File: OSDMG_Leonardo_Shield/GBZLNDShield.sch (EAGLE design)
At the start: 12 parts

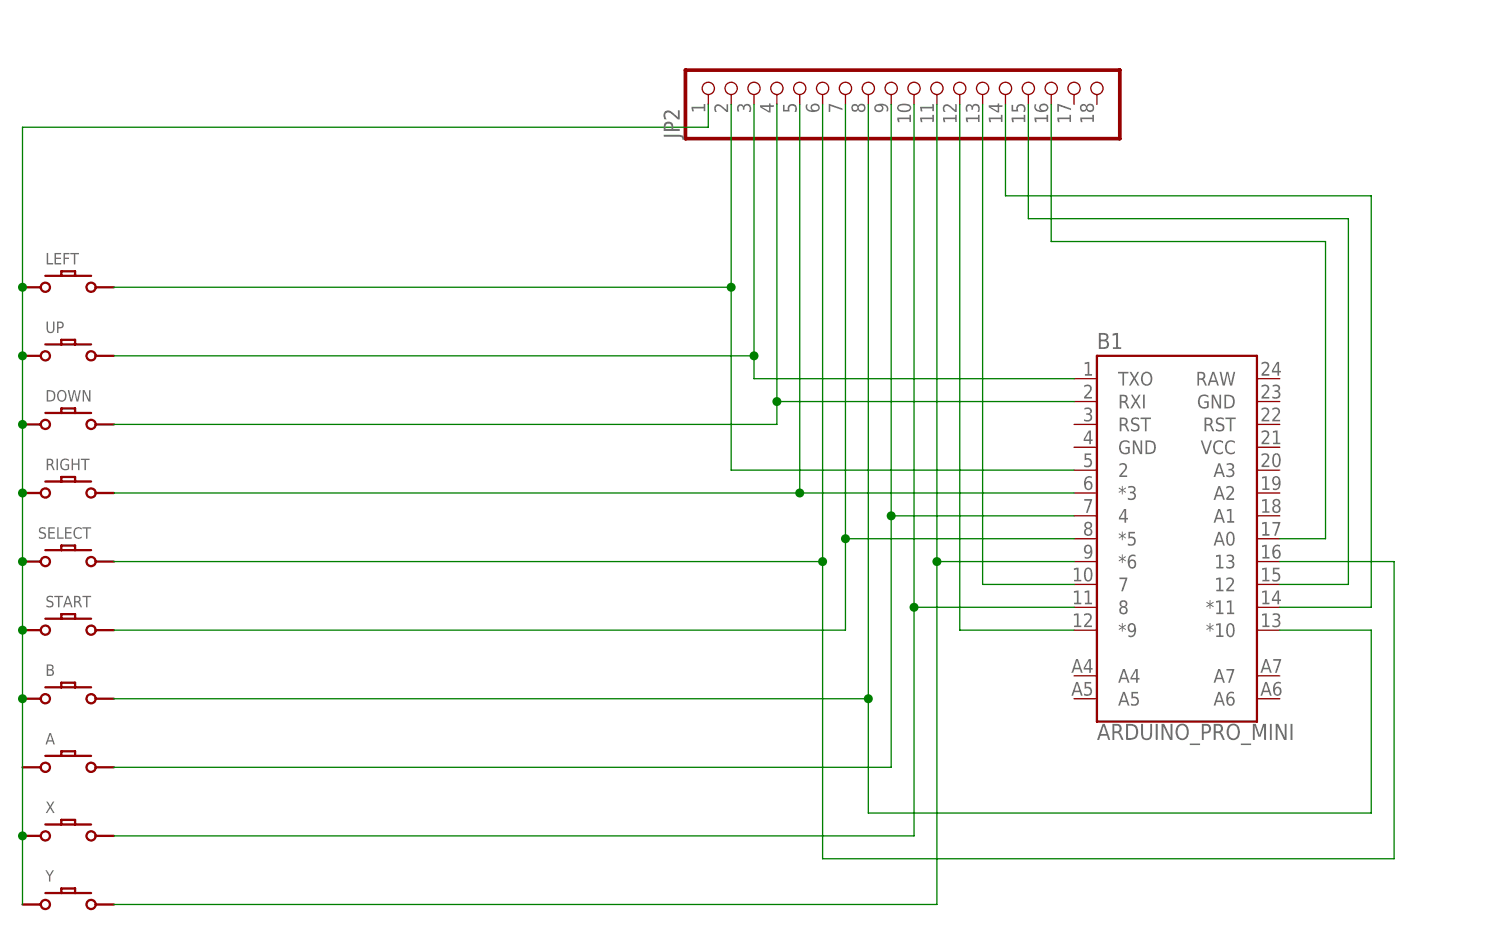
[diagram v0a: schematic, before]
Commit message: update board
5V and GND Pads and better placement of the leonardo
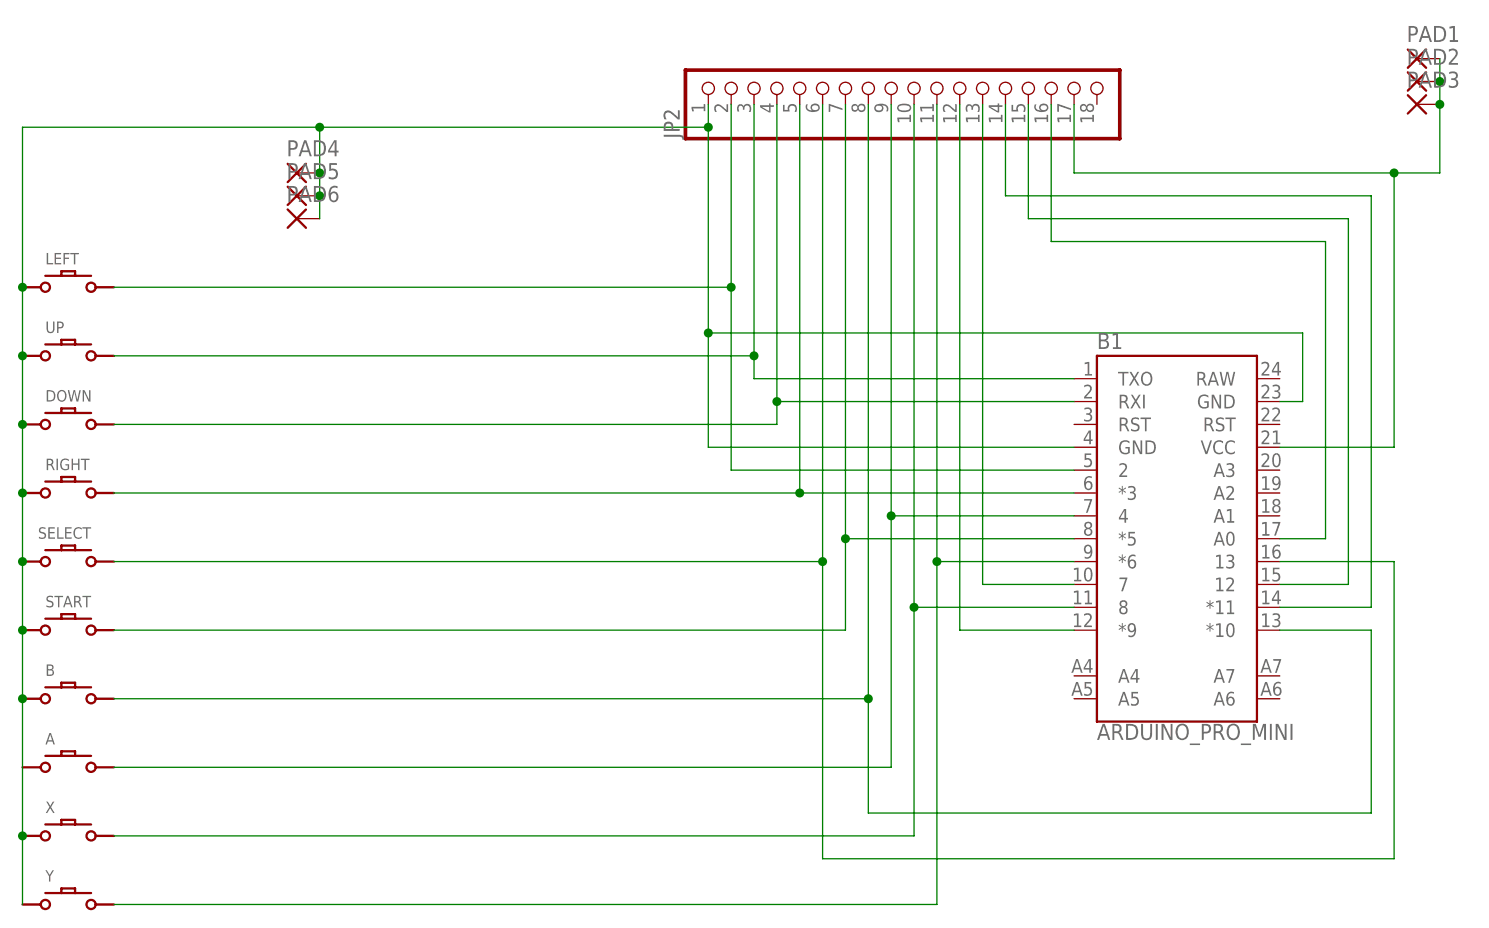
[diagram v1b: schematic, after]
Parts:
- added PAD1, PAD2, PAD3, PAD4, PAD5, PAD6: (no value), wirepad:SMD5
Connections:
- new net N$17: B1.VCC, JP2.17, PAD1.P, PAD2.P, PAD3.P
- net GND: now also B1.GND, B1.GND@2, PAD4.P, PAD5.P, PAD6.P
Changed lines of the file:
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@@
 <part name="JP2" library="adafruit" deviceset="PINHD-1X18" device="-BIG"/>
 <part name="B1" library="SparkFun-Boards" deviceset="ARDUINO_PRO_MINI" device=""/>
+<part name="PAD1" library="wirepad" library_urn="urn:adsk.eagle:library:412" deviceset="SMD5" device="" package3d_urn="urn:adsk.eagle:package:30841/1"/>
+<part name="PAD2" library="wirepad" library_urn="urn:adsk.eagle:library:412" deviceset="SMD5" device="" package3d_urn="urn:adsk.eagle:package:30841/1"/>
+<part name="PAD3" library="wirepad" library_urn="urn:adsk.eagle:library:412" deviceset="SMD5" device="" package3d_urn="urn:adsk.eagle:package:30841/1"/>
+<part name="PAD4" library="wirepad" library_urn="urn:adsk.eagle:library:412" deviceset="SMD5" device="" package3d_urn="urn:adsk.eagle:package:30841/1"/>
+<part name="PAD5" library="wirepad" library_urn="urn:adsk.eagle:library:412" deviceset="SMD5" device="" package3d_urn="urn:adsk.eagle:package:30841/1"/>
+<part name="PAD6" library="wirepad" library_urn="urn:adsk.eagle:library:412" deviceset="SMD5" device="" package3d_urn="urn:adsk.eagle:package:30841/1"/>
 </parts>
 <sheets>
@@
 <instance part="JP2" gate="A" x="109.22" y="91.44" rot="R90"/>
 <instance part="B1" gate="G$1" x="139.7" y="40.64"/>
+<instance part="PAD1" gate="1" x="167.64" y="93.98"/>
+<instance part="PAD2" gate="1" x="167.64" y="91.44"/>
+<instance part="PAD3" gate="1" x="167.64" y="88.9"/>
+<instance part="PAD4" gate="1" x="43.18" y="81.28"/>
+<instance part="PAD5" gate="1" x="43.18" y="78.74"/>
+<instance part="PAD6" gate="1" x="43.18" y="76.2"/>
 </instances>
 <busses>
@@
 <wire x1="12.7" y1="68.58" x2="12.7" y2="86.36" width="0.1524" layer="91"/>
 <pinref part="UP" gate="G$1" pin="P$1"/>
-<wire x1="12.7" y1="86.36" x2="88.9" y2="86.36" width="0.1524" layer="91"/>
+<wire x1="12.7" y1="86.36" x2="45.72" y2="86.36" width="0.1524" layer="91"/>
+<wire x1="45.72" y1="86.36" x2="88.9" y2="86.36" width="0.1524" layer="91"/>
 <wire x1="12.7" y1="60.96" x2="12.7" y2="68.58" width="0.1524" layer="91"/>
 <junction x="12.7" y="68.58"/>
@@
 <wire x1="88.9" y1="86.36" x2="88.9" y2="88.9" width="0.1524" layer="91"/>
 <pinref part="JP2" gate="A" pin="1"/>
+<pinref part="PAD6" gate="1" pin="P"/>
+<pinref part="PAD5" gate="1" pin="P"/>
+<wire x1="45.72" y1="76.2" x2="45.72" y2="78.74" width="0.1524" layer="91"/>
+<pinref part="PAD4" gate="1" pin="P"/>
+<wire x1="45.72" y1="78.74" x2="45.72" y2="81.28" width="0.1524" layer="91"/>
+<junction x="45.72" y="78.74"/>
+<wire x1="45.72" y1="81.28" x2="45.72" y2="86.36" width="0.1524" layer="91"/>
+<junction x="45.72" y="81.28"/>
+<junction x="45.72" y="86.36"/>
+<pinref part="B1" gate="G$1" pin="GND"/>
+<wire x1="129.54" y1="50.8" x2="88.9" y2="50.8" width="0.1524" layer="91"/>
+<wire x1="88.9" y1="50.8" x2="88.9" y2="63.5" width="0.1524" layer="91"/>
+<junction x="88.9" y="86.36"/>
+<pinref part="B1" gate="G$1" pin="GND@2"/>
+<wire x1="88.9" y1="63.5" x2="88.9" y2="86.36" width="0.1524" layer="91"/>
+<wire x1="152.4" y1="55.88" x2="154.94" y2="55.88" width="0.1524" layer="91"/>
+<wire x1="154.94" y1="55.88" x2="154.94" y2="63.5" width="0.1524" layer="91"/>
+<wire x1="154.94" y1="63.5" x2="88.9" y2="63.5" width="0.1524" layer="91"/>
+<junction x="88.9" y="63.5"/>
 </segment>
 </net>
@@
 </segment>
 </net>
+<net name="N$17" class="0">
+<segment>
+<pinref part="PAD1" gate="1" pin="P"/>
+<pinref part="PAD2" gate="1" pin="P"/>
+<wire x1="170.18" y1="93.98" x2="170.18" y2="91.44" width="0.1524" layer="91"/>
+<pinref part="PAD3" gate="1" pin="P"/>
+<wire x1="170.18" y1="91.44" x2="170.18" y2="88.9" width="0.1524" layer="91"/>
+<junction x="170.18" y="91.44"/>
+<wire x1="170.18" y1="88.9" x2="170.18" y2="81.28" width="0.1524" layer="91"/>
+<junction x="170.18" y="88.9"/>
+<pinref part="JP2" gate="A" pin="17"/>
+<wire x1="170.18" y1="81.28" x2="165.1" y2="81.28" width="0.1524" layer="91"/>
+<wire x1="165.1" y1="81.28" x2="129.54" y2="81.28" width="0.1524" layer="91"/>
+<wire x1="129.54" y1="81.28" x2="129.54" y2="88.9" width="0.1524" layer="91"/>
+<pinref part="B1" gate="G$1" pin="VCC"/>
+<wire x1="152.4" y1="50.8" x2="165.1" y2="50.8" width="0.1524" layer="91"/>
+<wire x1="165.1" y1="50.8" x2="165.1" y2="81.28" width="0.1524" layer="91"/>
+<junction x="165.1" y="81.28"/>
+</segment>
+</net>
 </nets>
 </sheet>
@@
 </schematic>
 </drawing>
+<compatibility>
+<note version="8.2" severity="warning">
+Since Version 8.2, EAGLE supports online libraries. The ids
+of those online libraries will not be understood (or retained)
+with this version.
+</note>
+<note version="8.3" severity="warning">
+Since Version 8.3, EAGLE supports URNs for individual library
+assets (packages, symbols, and devices). The URNs of those assets
+will not be understood (or retained) with this version.
+</note>
+<note version="8.3" severity="warning">
+Since Version 8.3, EAGLE supports the association of 3D packages
+with devices in libraries, schematics, and board files. Those 3D
+packages will not be understood (or retained) with this version.
+</note>
+</compatibility>
 </eagle>
